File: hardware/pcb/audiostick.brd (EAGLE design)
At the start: 84 x 34 mm, 61 parts, among them IC1 TPS73633MBDV, IC3 PCM5102ASW, IC5 AP22804W5, IC6 TINY13V-10SSU, J1 AVRISP6TH127, J2 AUDIO_JACK_3.5MM_PTH, J3 USB-B, T1 BC850

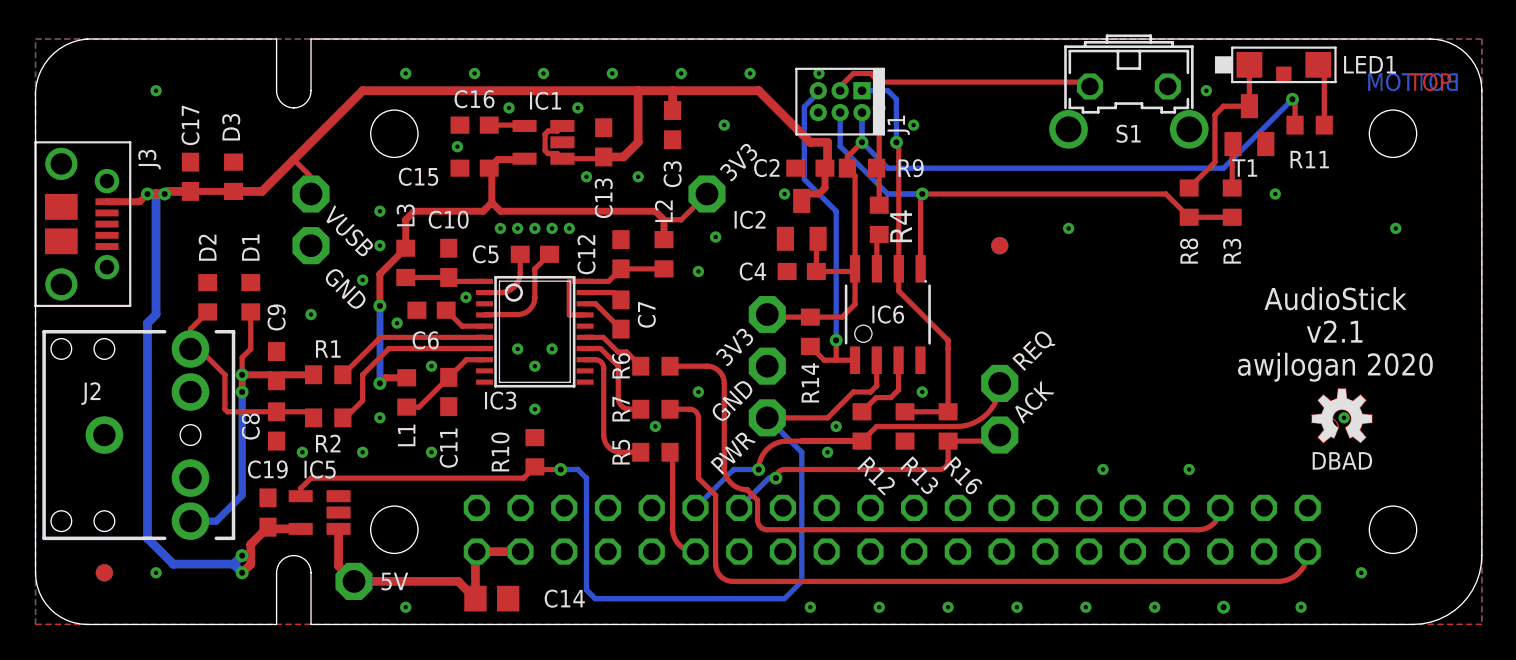
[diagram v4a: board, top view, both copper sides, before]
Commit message: Fix airwire and clearance
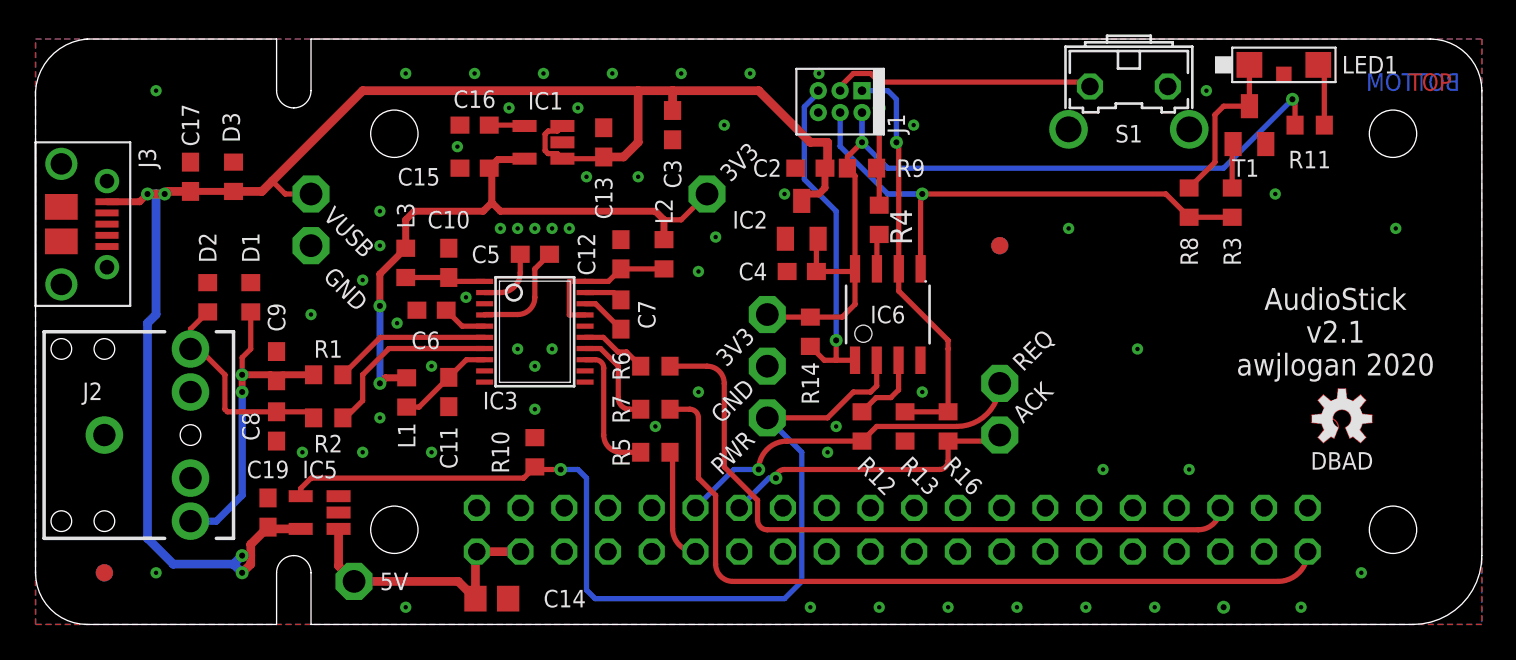
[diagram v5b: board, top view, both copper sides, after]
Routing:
- net S_REQ': track 24.7 -> 20.7 mm
- net +5V: track 98.4 -> 99.2 mm
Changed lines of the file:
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@@
 <via x="40" y="29" extent="1-16" drill="0.254"/>
 <via x="72" y="25" extent="1-16" drill="0.254"/>
-<via x="76" y="12" extent="1-16" drill="0.254"/>
+<via x="64" y="16" extent="1-16" drill="0.254"/>
 <via x="60" y="23" extent="1-16" drill="0.254"/>
 <via x="67" y="9" extent="1-16" drill="0.254"/>
@@
 <contactref element="C5" pad="2"/>
 <contactref element="IC3" pad="2"/>
-<wire x1="27.275" y1="19.275" x2="27" y2="19.275" width="0.3048" layer="1"/>
 <wire x1="27" y1="19.275" x2="26.0822" y2="19.275" width="0.3048" layer="1"/>
 <wire x1="28.15" y1="20.425" x2="28.15" y2="21.5" width="0.3048" layer="1"/>
@@
 <wire x1="39" y1="15" x2="36.85" y2="15" width="0.3048" layer="1"/>
 <wire x1="67.538" y1="5.5" x2="42.5" y2="5.5" width="0.3048" layer="1"/>
-<wire x1="41.9348" y1="7.2118875" x2="41.32334375" y2="7.82334375" width="0.3048" layer="1"/>
-<wire x1="41.32334375" y1="7.82334375" x2="41.3098875" y2="7.8368" width="0.3048" layer="1"/>
-<wire x1="41.3098875" y1="7.8368" x2="41.098" y2="7.8368" width="0.3048" layer="1"/>
-<wire x1="41.9348" y1="6.0652" x2="41.9348" y2="7.2118875" width="0.3048" layer="1"/>
-<wire x1="40" y1="8.9348" x2="40" y2="9.1466875" width="0.3048" layer="1"/>
 <wire x1="40" y1="9.1466875" x2="40" y2="14" width="0.3048" layer="1"/>
 <wire x1="42.5" y1="5.5" x2="41.9348" y2="6.0652" width="0.3048" layer="1" curve="-90"/>
-<wire x1="41.32334375" y1="7.82334375" x2="40" y2="9.1466875" width="0.3048" layer="1" curve="-90"/>
 <wire x1="39" y1="15" x2="40" y2="14" width="0.3048" layer="1" curve="-90"/>
 <wire x1="68.808" y1="6.77" x2="67.538" y2="5.5" width="0.3048" layer="1" curve="-90"/>
+<wire x1="41.9348" y1="6.0652" x2="41.9348" y2="7.2118875" width="0.3048" layer="1"/>
+<wire x1="41.9348" y1="7.2118875" x2="40" y2="9.1466875" width="0.3048" layer="1"/>
 </signal>
 <signal name="BCK">
@@
 <wire x1="45.5" y1="25" x2="44.5" y2="25" width="0.4064" layer="1"/>
 <wire x1="44.5" y1="25" x2="44.5" y2="24.6" width="0.4064" layer="1"/>
-<wire x1="15" y1="27" x2="19" y2="31" width="0.508" layer="1"/>
+<wire x1="13.75" y1="25.75" x2="19" y2="31" width="0.508" layer="1"/>
 <wire x1="19" y1="31" x2="35" y2="31" width="0.508" layer="1"/>
 <wire x1="35" y1="31" x2="37" y2="31" width="0.508" layer="1"/>
@@
 <wire x1="34.15" y1="27.15" x2="35" y2="28" width="0.508" layer="1"/>
 <wire x1="35" y1="28" x2="35" y2="31" width="0.508" layer="1"/>
-<wire x1="15" y1="27" x2="16" y2="26" width="0.3048" layer="1"/>
 <contactref element="IC5" pad="5"/>
 <contactref element="C17" pad="1"/>
 <contactref element="J3" pad="VBUS"/>
 <contactref element="D3" pad="2"/>
-<wire x1="9" y1="25.15" x2="8.75" y2="25.4" width="0.4064" layer="1"/>
 <wire x1="11.5" y1="25.15" x2="9" y2="25.15" width="0.4064" layer="1"/>
 <wire x1="4.15" y1="24.55" x2="6.05" y2="24.55" width="0.4064" layer="1"/>
@@
 <wire x1="7.65" y1="25.15" x2="7.5" y2="25" width="0.508" layer="1"/>
 <wire x1="11.5" y1="25.15" x2="13.15" y2="25.15" width="0.508" layer="1"/>
-<wire x1="13.15" y1="25.15" x2="15" y2="27" width="0.508" layer="1"/>
+<wire x1="13.15" y1="25.15" x2="13.75" y2="25.75" width="0.508" layer="1"/>
 <wire x1="11.5" y1="3.5" x2="12" y2="4" width="0.508" layer="16"/>
 <wire x1="11.5" y1="3.5" x2="12" y2="3" width="0.508" layer="16"/>
 <wire x1="12.5" y1="4" x2="12.5" y2="3.5" width="0.508" layer="1"/>
 <wire x1="12.5" y1="3.5" x2="12" y2="3" width="0.508" layer="1"/>
-<wire x1="16" y1="26" x2="16" y2="25" width="0" layer="19" extent="1-1"/>
+<wire x1="16" y1="25" x2="14.5" y2="25" width="0.3048" layer="1"/>
+<wire x1="14.5" y1="25" x2="13.75" y2="25.75" width="0.3048" layer="1"/>
 </signal>
 <signal name="SW">
 <contactref element="J1" pad="3"/>
 <contactref element="R9" pad="1"/>
-<wire x1="48.865" y1="26.485" x2="48.85" y2="26.5" width="0.3048" layer="1"/>
-<wire x1="48.85" y1="26.5" x2="48.925" y2="26.575" width="0.3048" layer="1"/>
 <wire x1="48.925" y1="26.575" x2="49" y2="26.65" width="0.3048" layer="1"/>
 <via x="49" y="30" extent="1-16" drill="0.35"/>
@@
 <wire x1="48.5" y1="32" x2="49" y2="31.5" width="0.3048" layer="1"/>
 <contactref element="R4" pad="1"/>
-<wire x1="49" y1="24.35" x2="49" y2="26.5" width="0.3048" layer="1"/>
 <wire x1="49" y1="26.5" x2="48.925" y2="26.575" width="0.3048" layer="1"/>
 <wire x1="49" y1="26.65" x2="49" y2="30" width="0.3048" layer="1"/>
@@
 <wire x1="60.984" y1="31.5" x2="61.2394" y2="31.2446" width="0.3048" layer="1"/>
 <wire x1="49" y1="31.5" x2="60.984" y2="31.5" width="0.3048" layer="1"/>
+<wire x1="48.85" y1="26.5" x2="48.925" y2="26.575" width="0.3048" layer="1"/>
+<wire x1="48.85" y1="26.5" x2="49" y2="26.35" width="0.3048" layer="1"/>
+<wire x1="49" y1="26.35" x2="49" y2="24.35" width="0.3048" layer="1"/>
 </signal>
 <signal name="S_REQ'">
@@
 <wire x1="43.65" y1="10.65" x2="48" y2="10.65" width="0.3048" layer="1"/>
 <wire x1="48" y1="10.65" x2="48.85" y2="11.5" width="0.3048" layer="1"/>
-<wire x1="56" y1="13.5" x2="56" y2="14" width="0.3048" layer="1"/>
 <wire x1="48.85" y1="11.5" x2="53.5" y2="11.5" width="0.3048" layer="1"/>
 <wire x1="56" y1="14" x2="53.5" y2="11.5" width="0.3048" layer="1" curve="-90"/>
 <wire x1="42" y1="9" x2="43.65" y2="10.65" width="0.3048" layer="1" curve="-90"/>
-<wire x1="44.5" y1="10.65" x2="48" y2="10.65" width="0.3048" layer="1"/>
 </signal>
 <signal name="N$13">

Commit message: Rationalised BOM a little
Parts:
- C14: device rcl:C0805 -> rcl:C0603
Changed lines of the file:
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@@
 <attribute name="VALUE" x="9.595" y="26.635" size="1.27" layer="27" rot="R270"/>
 </element>
-<element name="C14" library="rcl" library_urn="urn:adsk.eagle:library:334" package="C0805" package3d_urn="urn:adsk.eagle:package:23617/2" value="2u2" x="26.5" y="1.5" smashed="yes">
+<element name="C14" library="rcl" library_urn="urn:adsk.eagle:library:334" package="C0603" package3d_urn="urn:adsk.eagle:package:23616/2" value="2u2" x="26.5" y="1.5" smashed="yes">
 <attribute name="NAME" x="29.5" y="1.5" size="1.016" layer="25" font="vector" ratio="21" align="center-left"/>
-<attribute name="POPULARITY" value="88" x="26.5" y="1.5" size="1.016" layer="27" font="vector" ratio="21" display="off"/>
+<attribute name="POPULARITY" value="73" x="26.5" y="1.5" size="1.016" layer="27" font="vector" ratio="21" display="off"/>
 <attribute name="SPICEPREFIX" value="C" x="26.5" y="1.5" size="1.016" layer="27" font="vector" ratio="21" display="off"/>
 <attribute name="VALUE" x="25.23" y="-1.04" size="1.27" layer="27"/>
@@
 <wire x1="18.5" y1="2.5" x2="17.6" y2="3.4" width="0.508" layer="1"/>
 <wire x1="17.6" y1="3.4" x2="17.6" y2="5.55" width="0.508" layer="1"/>
-<wire x1="24.55" y1="2.5" x2="25.55" y2="1.5" width="0.508" layer="1"/>
-<wire x1="18.5" y1="2.5" x2="24.55" y2="2.5" width="0.508" layer="1"/>
-<wire x1="25.55" y1="1.5" x2="25.55" y2="4.152" width="0.508" layer="1"/>
+<wire x1="25.65" y1="1.5" x2="25.612134375" y2="2.504228125" width="0.508" layer="1"/>
+<wire x1="25.612134375" y1="2.504228125" x2="25.55" y2="4.152" width="0.508" layer="1"/>
 <wire x1="25.55" y1="4.152" x2="25.628" y2="4.23" width="0.508" layer="1"/>
+<wire x1="25.60790625" y1="2.5" x2="25.612134375" y2="2.504228125" width="0.508" layer="1"/>
+<wire x1="18.5" y1="2.5" x2="25.60790625" y2="2.5" width="0.508" layer="1"/>
 </signal>
 <signal name="+5V">

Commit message: Update BOM
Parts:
- C14: value 2u2 -> 4u7
- C17: value 1u -> 2u2
- C3: value 10u -> 4u7
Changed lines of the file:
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@@
 <attribute name="VALUE" x="13.325" y="8.405" size="1.27" layer="27" rot="R270"/>
 </element>
-<element name="C17" library="rcl" library_urn="urn:adsk.eagle:library:334" package="C0603" package3d_urn="urn:adsk.eagle:package:23616/2" value="1u" x="9" y="26" smashed="yes" rot="R90">
+<element name="C17" library="rcl" library_urn="urn:adsk.eagle:library:334" package="C0603" package3d_urn="urn:adsk.eagle:package:23616/2" value="2u2" x="9" y="26" smashed="yes" rot="R90">
 <attribute name="NAME" x="9" y="29" size="1.016" layer="25" font="vector" ratio="21" rot="R270" align="center"/>
 <attribute name="POPULARITY" value="73" x="9" y="26" size="1.778" layer="27" rot="R90" display="off"/>
@@
 <attribute name="VALUE" x="9.595" y="26.635" size="1.27" layer="27" rot="R270"/>
 </element>
-<element name="C14" library="rcl" library_urn="urn:adsk.eagle:library:334" package="C0603" package3d_urn="urn:adsk.eagle:package:23616/2" value="2u2" x="26.5" y="1.5" smashed="yes">
+<element name="C14" library="rcl" library_urn="urn:adsk.eagle:library:334" package="C0603" package3d_urn="urn:adsk.eagle:package:23616/2" value="4u7" x="26.5" y="1.5" smashed="yes">
 <attribute name="NAME" x="29.5" y="1.5" size="1.016" layer="25" font="vector" ratio="21" align="center-left"/>
 <attribute name="POPULARITY" value="73" x="26.5" y="1.5" size="1.016" layer="27" font="vector" ratio="21" display="off"/>
@@
 <attribute name="VALUE" x="23.405" y="20.365" size="1.27" layer="27" rot="R90"/>
 </element>
-<element name="C3" library="rcl" library_urn="urn:adsk.eagle:library:334" package="C0603" package3d_urn="urn:adsk.eagle:package:23616/2" value="10u" x="37" y="29" smashed="yes" rot="R270">
+<element name="C3" library="rcl" library_urn="urn:adsk.eagle:library:334" package="C0603" package3d_urn="urn:adsk.eagle:package:23616/2" value="4u7" x="37" y="29" smashed="yes" rot="R270">
 <attribute name="NAME" x="37" y="27" size="1.016" layer="25" font="vector" ratio="21" rot="R90" align="center-right"/>
 <attribute name="POPULARITY" value="73" x="37" y="29" size="1.778" layer="27" rot="R270" display="off"/>

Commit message: Revert to EVQ switch
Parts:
- removed S1: (no value), switch-omron:B3F-31XX
- added SW1: EVQP7, AudioStick:EVQP7L
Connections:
- net GND: now also SW1.2A, SW1.2B; no longer S1.1
- net SW: now also SW1.1A, SW1.1B; no longer S1.2
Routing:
- net SW: track 22.8 -> 35.6 mm, vias 1 -> 3
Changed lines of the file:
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@@
 <attribute name="VALUE" x="65.095" y="25.135" size="1.27" layer="27" rot="R270"/>
 </element>
-<element name="S1" library="switch-omron" library_urn="urn:adsk.eagle:library:377" package="B3F-31XX" package3d_urn="urn:adsk.eagle:package:27487/1" value="" x="63.5" y="30" smashed="yes" rot="R180">
-<attribute name="MF" value="" x="63.5" y="30" size="1.778" layer="27" rot="R180" display="off"/>
-<attribute name="MPN" value="B3F-3100" x="63.5" y="30" size="1.778" layer="27" rot="R180" display="off"/>
-<attribute name="NAME" x="63.5" y="28.5" size="1.016" layer="25" font="vector" ratio="21" rot="R180" align="center"/>
-<attribute name="OC_FARNELL" value="959704" x="63.5" y="30" size="1.778" layer="27" rot="R180" display="off"/>
-<attribute name="OC_NEWARK" value="36M3582" x="63.5" y="30" size="1.778" layer="27" rot="R180" display="off"/>
-<attribute name="POPULARITY" value="0" x="63.5" y="30" size="1.778" layer="27" rot="R180" display="off"/>
-<attribute name="VALUE" x="67.183" y="35.969" size="1.27" layer="27" ratio="10" rot="R180"/>
+<element name="SW1" library="AudioStick" package="EVQP7L" value="EVQP7" x="64.397" y="32.197" smashed="yes">
+<attribute name="NAME" x="64.397" y="28.737" size="1.016" layer="21" font="vector" ratio="21" align="bottom-center"/>
 </element>
 </elements>
@@
 <via x="69" y="1" extent="1-16" drill="0.35"/>
 <contactref element="C14" pad="2"/>
-<via x="68" y="31" extent="1-16" drill="0.254"/>
+<via x="61" y="29" extent="1-16" drill="0.254"/>
 <via x="40" y="29" extent="1-16" drill="0.254"/>
 <via x="72" y="25" extent="1-16" drill="0.254"/>
@@
 <contactref element="IC5" pad="2"/>
 <contactref element="T1" pad="2"/>
-<contactref element="S1" pad="1"/>
+<contactref element="SW1" pad="2A"/>
+<contactref element="SW1" pad="2B"/>
 </signal>
 <signal name="N$1">
@@
 <wire x1="49" y1="26.5" x2="48.925" y2="26.575" width="0.3048" layer="1"/>
 <wire x1="49" y1="26.65" x2="49" y2="30" width="0.3048" layer="1"/>
-<contactref element="S1" pad="2"/>
-<wire x1="60.984" y1="31.5" x2="61.2394" y2="31.2446" width="0.3048" layer="1"/>
-<wire x1="49" y1="31.5" x2="60.984" y2="31.5" width="0.3048" layer="1"/>
 <wire x1="48.85" y1="26.5" x2="48.925" y2="26.575" width="0.3048" layer="1"/>
 <wire x1="48.85" y1="26.5" x2="49" y2="26.35" width="0.3048" layer="1"/>
 <wire x1="49" y1="26.35" x2="49" y2="24.35" width="0.3048" layer="1"/>
+<contactref element="SW1" pad="1B"/>
+<contactref element="SW1" pad="1A"/>
+<wire x1="49" y1="31.5" x2="59.5" y2="31.5" width="0.3048" layer="1"/>
+<via x="61" y="33" extent="1-16" drill="0.35"/>
+<wire x1="59.5" y1="31.5" x2="61" y2="33" width="0.3048" layer="1"/>
+<wire x1="61" y1="33" x2="62.469" y2="33" width="0.3048" layer="1"/>
+<wire x1="62.469" y1="33" x2="62.547" y2="32.922" width="0.3048" layer="1"/>
+<via x="68" y="33" extent="1-16" drill="0.35"/>
+<wire x1="66.247" y1="32.922" x2="66.325" y2="33" width="0.3048" layer="1"/>
+<wire x1="66.325" y1="33" x2="68" y2="33" width="0.3048" layer="1"/>
+<wire x1="63.978475" y1="30.2866" x2="64.815525" y2="30.2866" width="0.3048" layer="16"/>
+<wire x1="61" y1="33" x2="61.265075" y2="33" width="0.3048" layer="16"/>
+<wire x1="67.528925" y1="33" x2="68" y2="33" width="0.3048" layer="16"/>
+<wire x1="61.265075" y1="33" x2="63.978475" y2="30.2866" width="0.3048" layer="16"/>
+<wire x1="64.815525" y1="30.2866" x2="67.528925" y2="33" width="0.3048" layer="16"/>
 </signal>
 <signal name="S_REQ'">
